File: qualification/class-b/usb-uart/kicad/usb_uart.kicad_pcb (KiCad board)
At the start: 4 copper layers, 45 x 35.7 mm, 32 parts, among them J1 TYPE-C-31-M-12, J2 UART1, J3 FLOW1, J4 RS485, U1 CH342F, U2 LDO, U3 THVD1450D

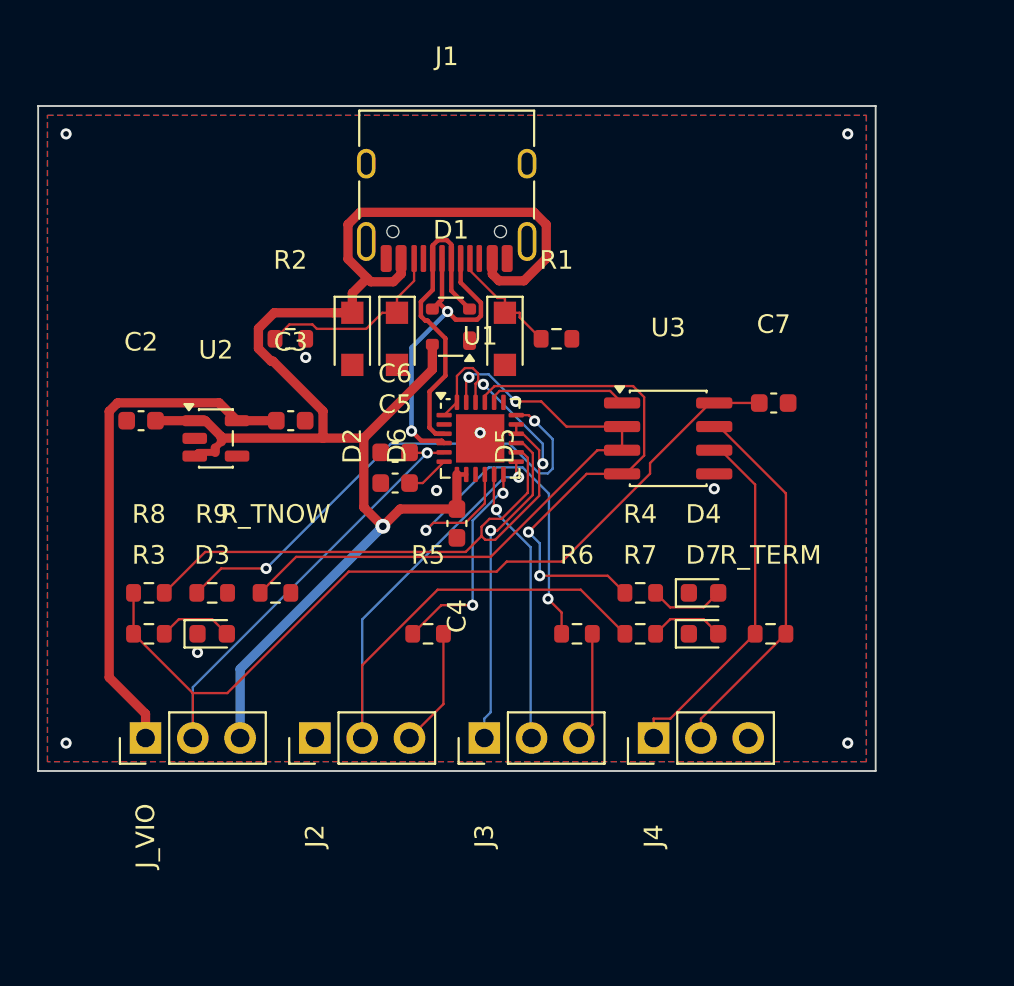
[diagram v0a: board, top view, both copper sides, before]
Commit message: SYN-66 - Switchable RS-485 termination, A/B surge protection, qualification matrix and hashes
Address the review of #103.

Board: R_TERM now sits behind a 2-pin jumper (J_TERM), so the board can be used away from the ends of a bus. A and B get 10 ohm series resistors and a Bourns CDSOT23-SM712 TVS array on the bus side, following TI's 1 kV surge circuit for the THVD1450 (SLLSEY3E fig. 37). The series resistors matter: the THVD1450 bus pins are rated +/-18 V and the SM712 clamps at 19 V to 26 V. Not surge-tested; the resistors are generic 0603.

Registry: add header_1x2 and cdsot23_sm712, and tag the THVD1450 A/B pins rs485_a and rs485_b for the RS-485 checks in #140.

Evidence: QUALIFICATION.md separates what Synth and KiCad checked from what needs SI/PI/RF or manufacturer review, SHA256SUMS records the artifact hashes, and reports/ holds the release gate and DRC records.

The revised board routes with 0 open nets but does not pass the release gate: KiCad reports 2 unconnected ground-pour items in every completed route. This is disclosed in the README and the matrix, not fixed. Needs absmach/synth#139 and #140 for the fabrication note and the RS-485 checks.

Signed-off-by: nyagamunene <stevenyaga2014@gmail.com>
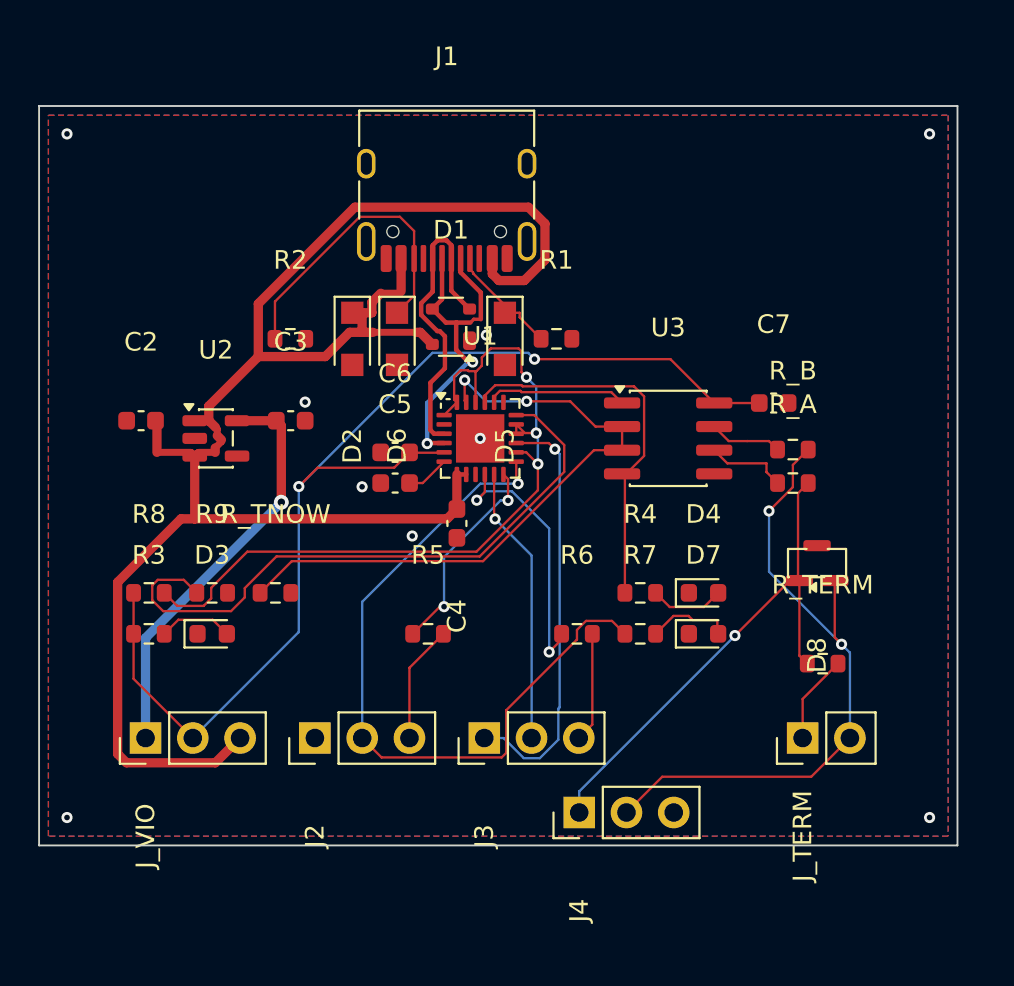
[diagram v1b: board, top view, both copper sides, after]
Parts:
- added D8: TVS, Package_TO_SOT_SMD:SOT-23, F.Cu at (41.9, 24.0)
- added J_TERM: TERM, Connector_PinHeader_2.54mm:PinHeader_1x02_P2.54mm_Vertical, F.Cu at (41.1, 33.4)
- added R_A: 10ohm, Resistor_SMD:R_0603_1608Metric, F.Cu at (40.6, 19.7)
- added R_B: 10ohm, Resistor_SMD:R_0603_1608Metric, F.Cu at (40.6, 17.9)
- moved J4 5.66 mm to (29.1, 37.4)
- moved R_TERM 3.22 mm to (42.2, 29.4)
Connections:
- J4 pad 1: RS485_A -> RS485_A_BUS
- J4 pad 2: RS485_B -> RS485_B_BUS
- R_TERM pad 1: RS485_A -> RS485_A_BUS
- R_TERM pad 2: RS485_B -> RS485_TERM
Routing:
- net RS485_B_BUS: track 0.00 -> 35.4 mm, vias 0 -> 2
- net RS485_A_BUS: track 0.00 -> 27.7 mm, vias 0 -> 1
- net RS485_B: track 20.4 -> 3.91 mm
- net RS485_A: track 19.4 -> 4.41 mm
- net VBUS: track 85.3 -> 98.0 mm, vias 1 -> 0
- net CTS1_MCU: track 21.8 -> 14.4 mm
- net TXD0: track 28.0 -> 20.6 mm, vias 2 -> 0
- net CTS0_LOW: track 27.3 -> 34.1 mm, vias 2 -> 0
- net VIO: track 68.8 -> 62.4 mm, vias 1 -> 2
- net CC2: track 10.6 -> 16.5 mm
- net +3V3: track 27.9 -> 22.3 mm, vias 0 -> 1
- net DTR1: track 17.7 -> 22.8 mm
- net RS485_TERM: track 0.00 -> 4.79 mm
- net MODEM_IDLE: track 45.0 -> 43.0 mm, vias 2 -> 3
- net LED_TX1: track 4.02 -> 4.57 mm
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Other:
- board size 45 x 35.7 mm -> 49.3 x 39.7 mm

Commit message: SYN-66 - Align the header row and re-route the board
The five headers now sit in one straight row at the bottom edge. Revision B had J4 pushed 4 mm out of the row because J_TERM was the only header without the bottom-edge hint and sat too close to it.

The aligned row did not route until J4 was turned 180 degrees, so RS-485 A (pin 1) is on the side the signals arrive from, and D8 was moved beside J4. FreeRouting then connects all 29 nets with 0 open. KiCad still reports the same 2 unconnected ground-pour items, so the release gate still says validation_failed; this is disclosed in the README and the matrix.

The board is 50.5 x 36.2 mm (revision A: 45.1 x 35.8). With the reference-label placement of absmach/synth#144 (not merged) KiCad reports no label overlap and no label clipped by the board edge: 51 warnings instead of 76.

Refreshed: the routed board, the release and routing records, the render, SHA256SUMS and the numbers in the README and the matrix.
Signed-off-by: nyagamunene <stevenyaga2014@gmail.com>
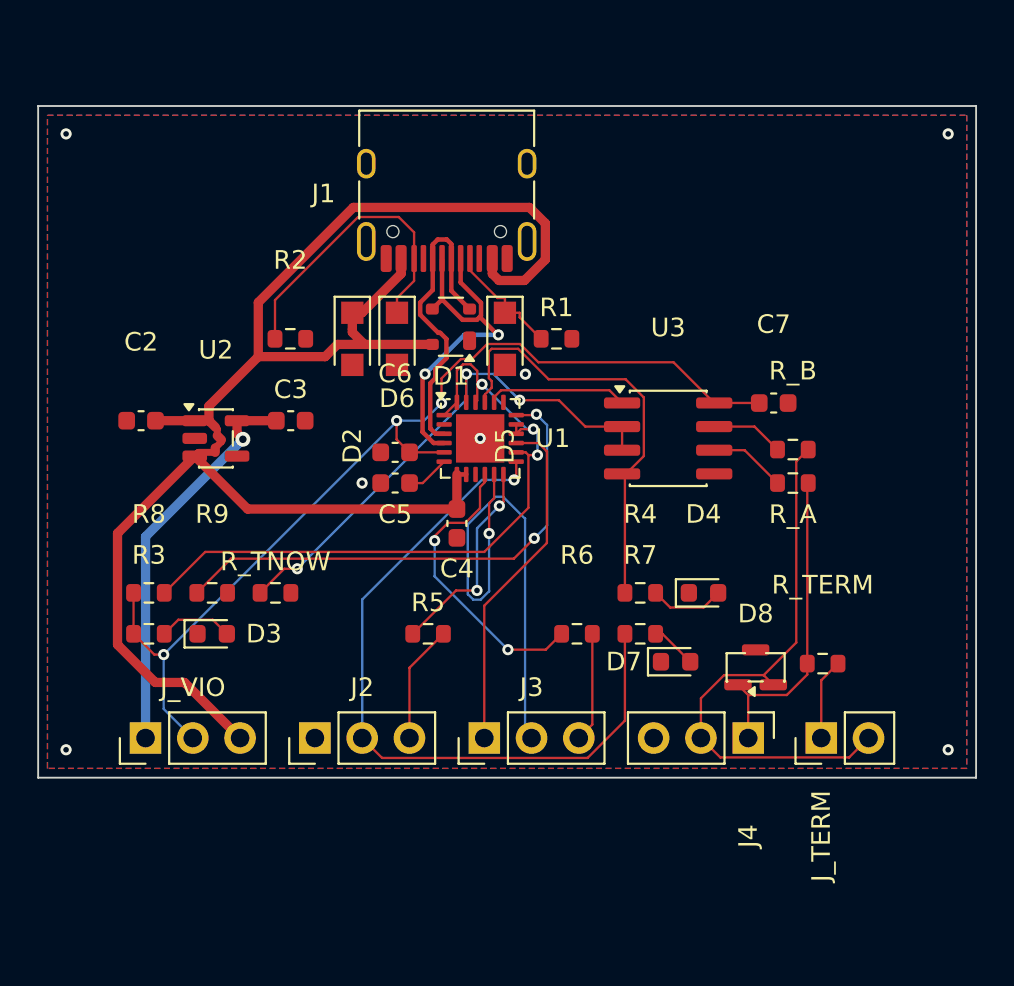
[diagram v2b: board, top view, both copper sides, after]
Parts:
- moved J4 9.92 mm to (38.2, 33.4), turned to 270 degrees
- moved D8 6.50 mm to (38.6, 29.6)
- moved D7 2.12 mm to (34.3, 29.3)
- moved J_TERM 1.00 mm to (42.1, 33.4)
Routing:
- net RTS1: track 15.0 -> 27.7 mm
- net RS485_A_BUS: track 27.7 -> 17.0 mm, vias 1 -> 0
- net VIO: track 62.4 -> 54.3 mm, vias 2 -> 3
- net CTS0_LOW: track 34.1 -> 27.6 mm, vias 0 -> 2
- net VBUS: track 98.0 -> 91.8 mm
- net RS485_B_BUS: track 35.4 -> 29.7 mm, vias 2 -> 0
- net TNOW0: track 34.6 -> 29.1 mm, vias 2 -> 3
- net MODEM_IDLE: track 43.0 -> 38.3 mm
- net DTR1: track 22.8 -> 18.6 mm, vias 1 -> 0
- net TXD0: track 20.6 -> 23.5 mm
- net LED_TX1: track 4.57 -> 2.48 mm
- net CTS1_MCU: track 14.4 -> 15.9 mm
- net USB_DN: track 18.7 -> 19.9 mm
- net +3V3: track 22.3 -> 21.5 mm
- net GND: vias 9 -> 7
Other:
- board size 49.3 x 39.7 mm -> 50.4 x 36.1 mm

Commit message: SYN-66 - Fix the floating ground pins and the clearance mismatch, board passes the release gate
C4 and D1 had their ground pin in a top-layer pour piece with no via to the ground planes; KiCad reported them as the 2 unconnected items. Moving C4 1 mm left lets the router place the stitching vias. The board now routes with 0 open nets, DRC 0 errors and 0 unconnected, and passes Synth's release gate. The 63 clearance errors after a KiCad re-save came from the project file giving net classes KiCad's 0.2 mm default instead of the 0.127 mm the router uses (PR #154, not merged yet). README, qualification matrix, reports, render and hashes are updated.

Signed-off-by: nyagamunene <stevenyaga2014@gmail.com>
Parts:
- moved C4 0.95 mm to (21.6, 21.9)
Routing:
- net VIO: track 54.3 -> 80.8 mm, vias 3 -> 1
- net TNOW0: track 29.1 -> 42.3 mm
- net RTS1: track 27.7 -> 15.1 mm, vias 1 -> 0
- net CTS0_LOW: track 27.6 -> 37.5 mm
- net TXD1: track 39.3 -> 31.7 mm, vias 1 -> 0
- net VBUS: track 91.8 -> 84.9 mm
- net CTS1_MCU: track 15.9 -> 12.6 mm
- net USB_DP: track 17.1 -> 14.3 mm, vias 0 -> 2
- net USB_DN: track 19.9 -> 17.4 mm, vias 2 -> 0
- net MODEM_IDLE: track 38.3 -> 36.3 mm
- net RXD1_MCU: track 11.2 -> 13.1 mm
- net DTR1: track 18.6 -> 17.6 mm, vias 0 -> 1
- net TXD0: track 23.5 -> 22.7 mm
- net GND: vias 7 -> 6

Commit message: SYN-66 - Use the Amphenol USB-C connector with its 3D model, centre it, add mounting holes, re-route
The HRO TYPE-C-31-M-12 has no 3D model anywhere in KiCad's library, and the GCT USB4105 puts its NPTH holes 0.175 mm from its pads, under JLCPCB's 0.2 mm. The board now uses the Amphenol 12401610E4#2A (new registry part, datasheet not read: the manufacturer's site refuses requests). J1 is centred on the top edge, four M2.5 mounting holes are added, VBUS is routed at 0.3 mm to fit the connector's 0.3 mm contacts, and the board is re-routed: 29 nets, 0 open, DRC 0 errors and 0 unconnected, release gate passed. README, qualification matrix, reports, render and hashes are updated; they depend on PR #154 and PR #162, which are not merged yet.

Signed-off-by: nyagamunene <stevenyaga2014@gmail.com>
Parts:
- added H1: (no value), MountingHole:MountingHole_2.5mm, F.Cu at (2.85, 2.85)
- added H2: (no value), MountingHole:MountingHole_2.5mm, F.Cu at (47.8, 2.85)
- added H3: (no value), MountingHole:MountingHole_2.5mm, F.Cu at (2.85, 24.5)
- added H4: (no value), MountingHole:MountingHole_2.5mm, F.Cu at (47.8, 24.5)
- J1: value TYPE-C-31-M-12 -> 12401610E4#2A; footprint Connector_USB:USB_C_Receptacle_HRO_TYPE-C-31-M-12 -> Connector_USB:USB_C_Receptacle_Amphenol_12401610E4-2A
- moved R2 4.29 mm to (16.9, 14.8)
- moved D2 4.29 mm to (20.2, 14.8)
- moved D5 4.29 mm to (28.4, 14.8)
- moved D6 4.29 mm to (22.6, 14.8)
- moved R1 4.29 mm to (31.1, 14.8)
- moved D1 4.29 mm to (25.5, 14.1)
- moved J1 3.89 mm to (25.2, 5.73)
- moved J2 2.80 mm to (14.9, 36.2)
- moved J3 2.80 mm to (24.0, 36.2)
- moved J4 2.80 mm to (38.2, 36.2)
- moved J_TERM 2.80 mm to (42.1, 36.2)
- moved J_VIO 2.80 mm to (5.82, 36.2)
- moved R_TERM 2.80 mm to (42.2, 32.2)
- moved C4 2.80 mm to (21.6, 24.7)
- moved C5 2.80 mm to (19.2, 22.5)
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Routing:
- net MODEM_IDLE: track 36.3 -> 82.3 mm, vias 3 -> 2
- net VIO: track 80.8 -> 58.8 mm
- net CTS0_LOW: track 37.5 -> 23.2 mm
- net TNOW0: track 42.3 -> 32.5 mm
- net USB_DP: track 14.3 -> 19.3 mm, vias 2 -> 3
- net CC2: track 16.4 -> 20.9 mm, vias 0 -> 2
- net TXD0: track 22.7 -> 20.6 mm
- net RTS1: track 15.1 -> 16.8 mm
- net USB_DN: track 17.4 -> 15.7 mm, vias 0 -> 2
- net VBUS: track 84.9 -> 83.7 mm
- net RXD1_MCU: track 13.1 -> 12.2 mm
- net DTR1: track 17.6 -> 18.2 mm
- net CTS1_MCU: track 12.6 -> 12.1 mm, vias 2 -> 0
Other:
- board size 50.4 x 36.1 mm -> 50.4 x 38.3 mm
- net class VBUS_FINE added: clearance 0.127, trace_width 0.3, via_dia 0.6, via_drill 0.3

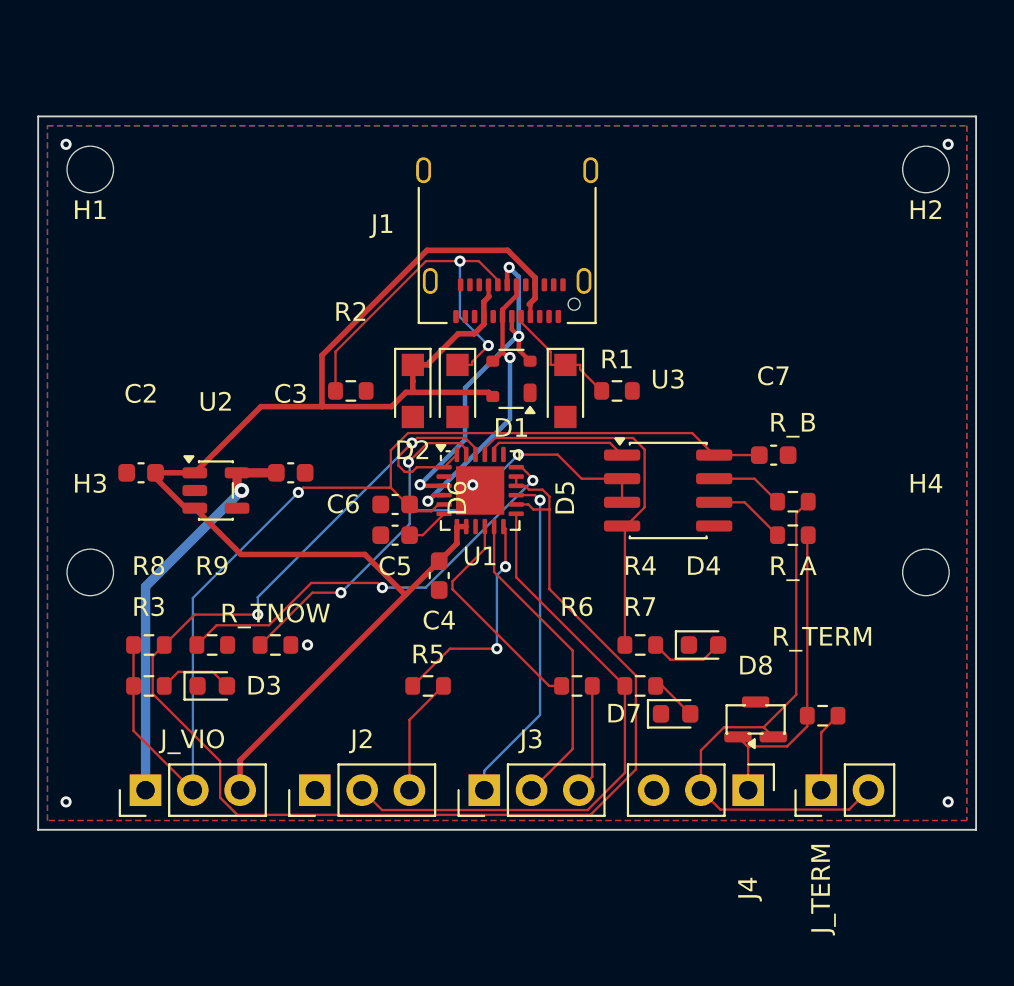
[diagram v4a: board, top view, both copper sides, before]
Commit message: SYN-66 - Use M3 mounting holes, re-route, and replace every picture
The four mounting holes are now M3 (3.2 mm), a new registry part. The board is re-placed and re-routed (the first M3 layout that passed was the 23rd tried): 29 nets, 0 open, DRC 0 errors and 0 unconnected, release gate passed. All pictures are new: 3D top, angled and bottom views, top and bottom copper, and the schematic; the STEP, reports, hashes, README and qualification matrix match the board. The USB pair is badly skewed (13.5 mm) and the docs say so.

Signed-off-by: nyagamunene <stevenyaga2014@gmail.com>
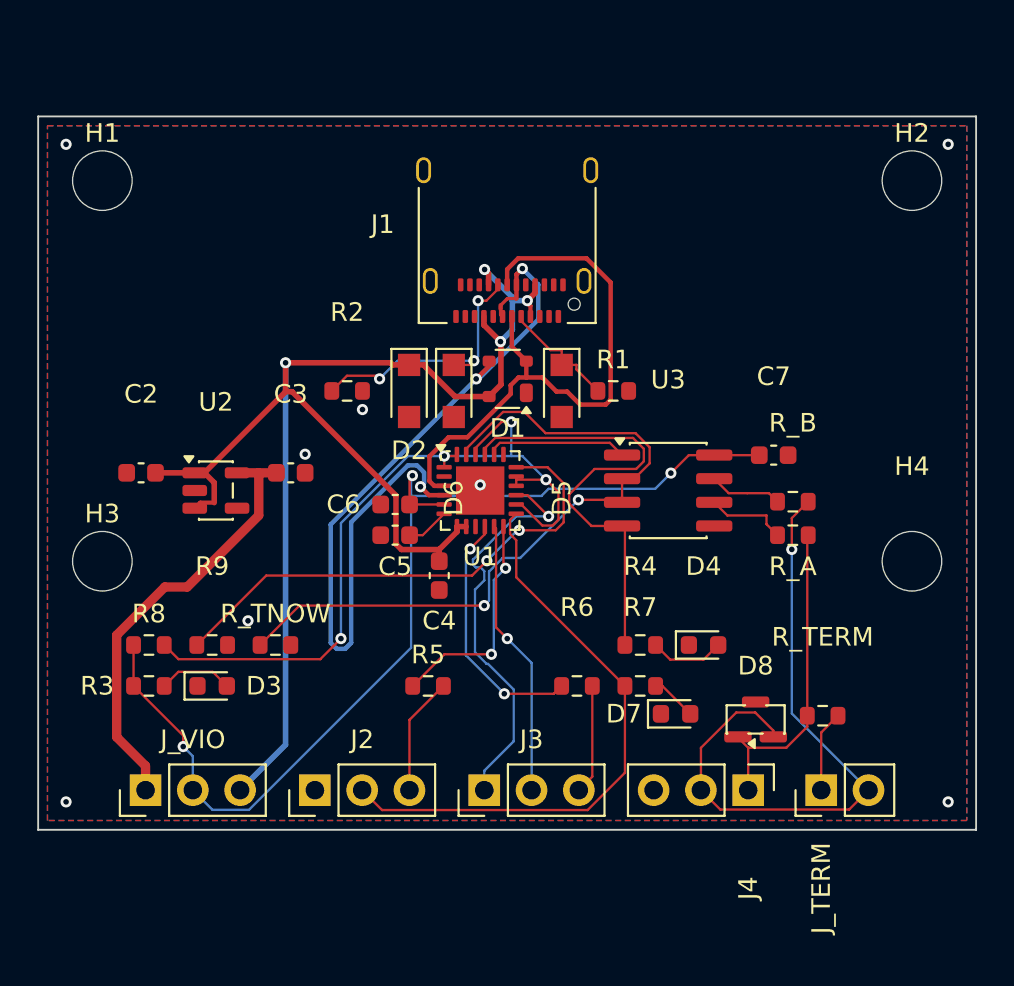
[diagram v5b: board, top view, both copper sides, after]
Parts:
- H1, H2, H3, H4: footprint MountingHole:MountingHole_2.5mm -> MountingHole:MountingHole_3.2mm_M3
- moved H4 0.96 mm to (47.0, 23.9)
- moved H2 0.96 mm to (47.0, 3.45)
- moved H3 0.88 mm to (3.50, 23.9)
- moved H1 0.88 mm to (3.50, 3.45)
- moved R2 0.20 mm to (16.6, 14.8)
- moved D1 0.20 mm to (25.3, 14.1)
- moved D2 0.20 mm to (20.0, 14.8)
- moved D5 0.20 mm to (28.2, 14.8)
- moved D6 0.20 mm to (22.4, 14.8)
- moved R1 0.20 mm to (30.9, 14.8)
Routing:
- net MODEM_IDLE: track 82.3 -> 42.9 mm, vias 2 -> 4
- net USB_DN: track 15.7 -> 45.3 mm, vias 2 -> 3
- net USB_DP: track 19.3 -> 31.8 mm, vias 3 -> 0
- net TNOW0: track 32.5 -> 39.3 mm, vias 3 -> 2
- net CC2: track 20.9 -> 14.5 mm, vias 2 -> 3
- net RS485_B_BUS: track 29.7 -> 35.1 mm, vias 0 -> 1
- net VBUS: track 83.7 -> 78.5 mm, vias 0 -> 4
- net TXD0: track 20.6 -> 25.1 mm
- net CTS0_LOW: track 23.2 -> 27.4 mm
- net DTR1: track 18.2 -> 21.8 mm
- net +3V3: track 21.4 -> 23.7 mm, vias 1 -> 0
- net RTS1: track 16.8 -> 15.0 mm, vias 0 -> 1
- net VIO: track 58.8 -> 57.3 mm, vias 1 -> 3
- net CTS1_MCU: track 12.1 -> 13.5 mm, vias 0 -> 2
- net GND: vias 6 -> 8
